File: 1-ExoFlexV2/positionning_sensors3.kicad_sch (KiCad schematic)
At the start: 34 parts, among them U63 SN74LVC1G08DBVR, U64 SN74LVC1G08DBVR, U65 SN74LVC3G14DCUT_V2

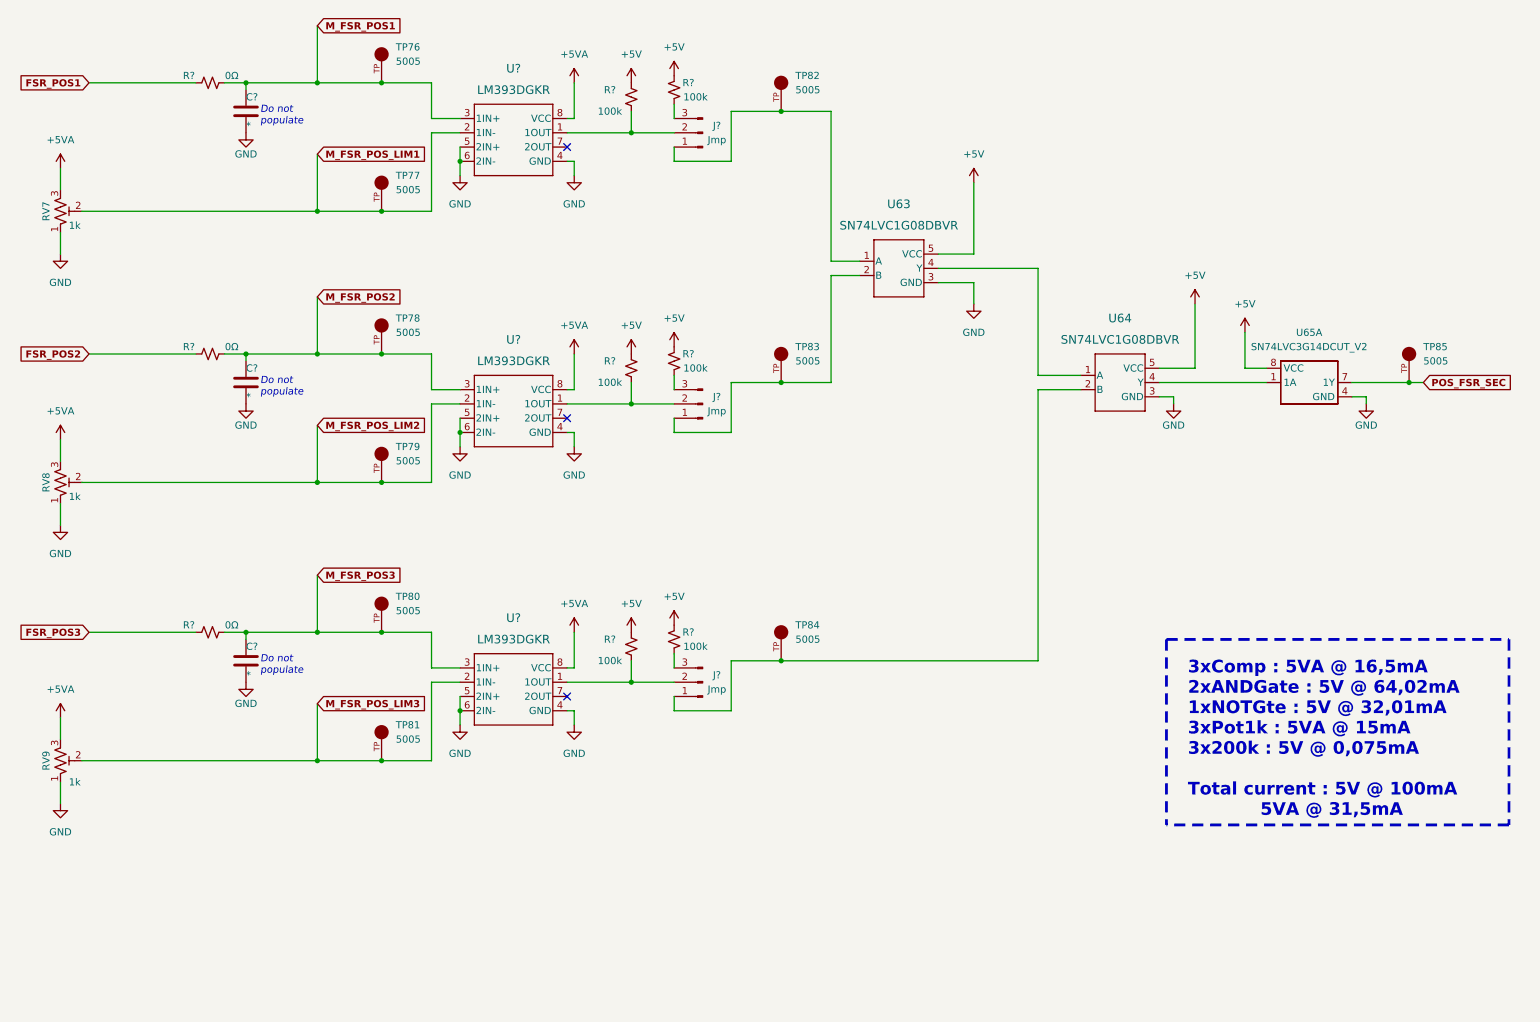
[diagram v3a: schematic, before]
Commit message: Test points et notes
- Ajout de tous les tests point nécessaires
-  Ajoute des sections de notes dans chaque page
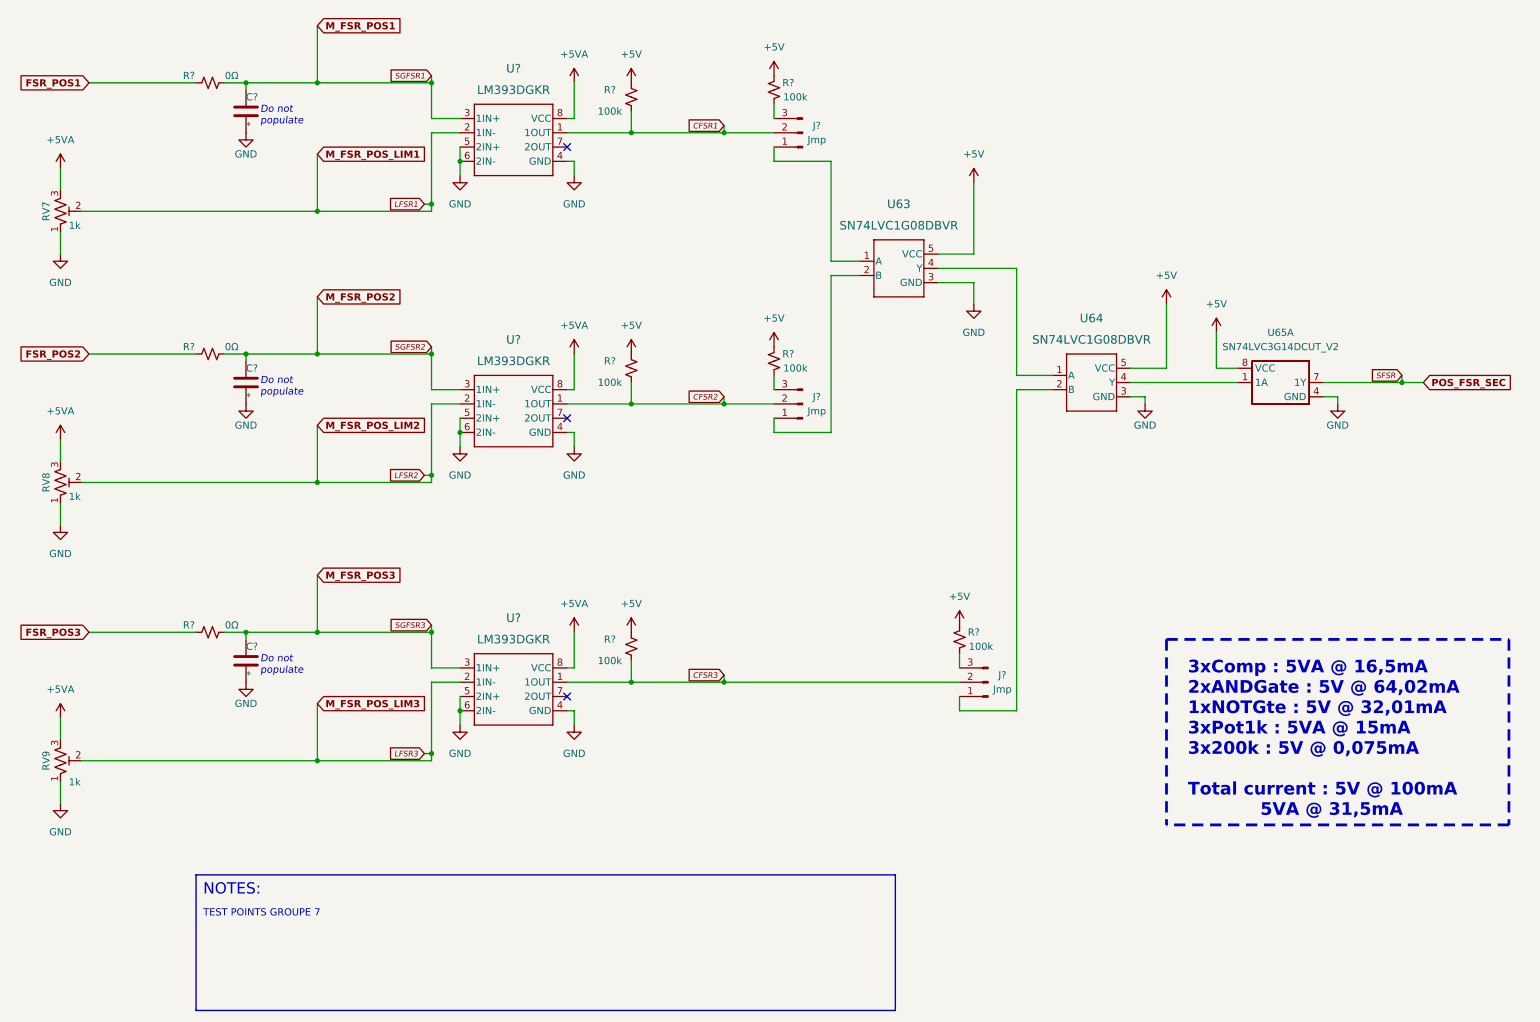
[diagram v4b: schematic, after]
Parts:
- removed TP76, TP77, TP78, TP79, TP80, TP81, TP82, TP83, TP84, TP85: 5005, FootPrint:KEYSTONE_5005, symbol SymLib:5005
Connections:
- net CFSR3: now reaches J?.2 (Pin_2), R?.2, U?.1 (1OUT)
- net CFSR2: now reaches J?.2 (Pin_2), R?.2, U?.1 (1OUT)
- net CFSR1: now reaches J?.2 (Pin_2), R?.2, U?.1 (1OUT)
- net M_FSR_POS_LIM1 renamed LFSR1
- net M_FSR_POS_LIM2 renamed LFSR2
- net M_FSR_POS_LIM3 renamed LFSR3
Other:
- note added: "NOTES:"
- note added: "TEST POINTS GROUPE 7"
- moved on the sheet: J?, R?, U64, U65A

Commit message: Schématisation terminée
- Schéma terminé
- Passage vers le PCB
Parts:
- C49, C50, C51: renamed from C?; value * -> 10nF 10V X5R; footprint Capacitor_SMD:C_0805_2012Metric -> Capacitor_SMD:C_01005_0402Metric; DESCRIPTION (none) -> 10000 pF ±10% 10V Ceramic Capacitor X5R 01005 (0402 Metric); MANUFACTURER (none) -> Murata Electronics; NOTES (none) -> DO NOT POPULATE; PACKAGE (none) -> 01005 (0402 Metric); PART NUMBER (none) -> GRM022R61A103KE19L; TYPE (none) -> SMD
- J106, J107, J108: renamed from J?; value Jmp -> Jumper; footprint (none) -> Connector_PinSocket_2.54mm:PinSocket_1x03_P2.54mm_Vertical; DESCRIPTION (none) -> CONN HEADER VERT 3POS 2.54MM; MANUFACTURER (none) -> Würth Elektronik; PACKAGE (none) -> Square 0.100" (2.54mm); PART NUMBER (none) -> 61300311121; TYPE (none) -> Through Hole
- R155, R156, R157: renamed from R?; DESCRIPTION (none) -> 0 Ohms Jumper Chip Resistor 0805 (2012 Metric) Automotive A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; MANUFACTURER (none) -> Panasonic Electronic Components; PACKAGE (none) -> 0805 (2012 Metric); PART NUMBER (none) -> ERJ-6GEY0R00V; TYPE (none) -> SMD
- R158, R159, R160, R161, R162, R163: renamed from R?; value 100k -> 100k 5% 1/8W; DESCRIPTION (none) -> 100 kOhms ±5% 0.125W, 1/8W Chip Resistor 0805 (2012 Metric)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; MANUFACTURER (none) -> Panasonic Electronic Components; PACKAGE (none) -> 0805 (2012 Metric); PART NUMBER (none) -> ERJ-6GEYJ104V; TYPE (none) -> SMD
- RV30: renamed from RV7; value 1k -> Trim 1k; DESCRIPTION (none) -> Trimmer 1k 0,5W PC PIN TOP; MANUFACTURER (none) -> Bourns Inc.; PACKAGE (none) -> Rectangular - 0.275" x 0.260" Face; PART NUMBER (none) -> 3362P-1-102LF; TYPE (none) -> Through Hole
- RV31: renamed from RV8; value 1k -> Trim 1k; DESCRIPTION (none) -> Trimmer 1k 0,5W PC PIN TOP; MANUFACTURER (none) -> Bourns Inc.; PACKAGE (none) -> Rectangular - 0.275" x 0.260" Face; PART NUMBER (none) -> 3362P-1-102LF; TYPE (none) -> Through Hole
- RV32: renamed from RV9; value 1k -> Trim 1k; DESCRIPTION (none) -> Trimmer 1k 0,5W PC PIN TOP; MANUFACTURER (none) -> Bourns Inc.; PACKAGE (none) -> Rectangular - 0.275" x 0.260" Face; PART NUMBER (none) -> 3362P-1-102LF; TYPE (none) -> Through Hole
- U79, U80, U81: renamed from U?; value LM393DGKR -> COMP; footprint DGK8 -> FootPrint:DGK8; DESCRIPTION (none) -> Comparator General Purpose Open-Collector, Rail-to-Rail 8-V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; MANUFACTURER (none) -> Texas Instruments; PACKAGE (none) -> 8-TSSOP, 8-MSOP (0.118", 3.00mm Width); PART NUMBER (none) -> LM393DGKR; TYPE (none) -> SMD
- U82: renamed from U63; value SN74LVC1G08DBVR -> AND Gate; DESCRIPTION (none) -> AND Gate IC 1 Channel SOT-23-5; MANUFACTURER (none) -> Texas Instruments; PACKAGE (none) -> SC-74A, SOT-753; PART NUMBER (none) -> SN74LVC1G08DBVR; TYPE (none) -> SMD
- U83: renamed from U64; value SN74LVC1G08DBVR -> AND Gate; DESCRIPTION (none) -> AND Gate IC 1 Channel SOT-23-5; MANUFACTURER (none) -> Texas Instruments; PACKAGE (none) -> SC-74A, SOT-753; PART NUMBER (none) -> SN74LVC1G08DBVR; TYPE (none) -> SMD
- U84: renamed from U65; value SN74LVC3G14DCUT_V2 -> Inverter; DESCRIPTION (none) -> Inverter IC 3 Channel Schmitt Trigger 8-VSSOP; MANUFACTURER (none) -> Texas Instruments; PACKAGE (none) -> 8-VFSOP (0.091", 2.30mm Width); PART NUMBER (none) -> SN74LVC3G14DCUT; TYPE (none) -> SMD
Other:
- note added: "3xComp : 5VA @ 77,4mA 2xANDGate : 5V @ 64,02mA 1xNOTGte : 5V @ 32,01mA 3xPot1k : 5VA @ 300mA 6x100k : 5V @ 0,3mA Total current : 5V @ 101mA 5VA @ 382mA"
- note removed: "3xComp : 5VA @ 16,5mA 2xANDGate : 5V @ 64,02mA 1xNOTGte : 5V @ 32,01mA 3xPot1k : 5VA @ 15mA 3x200k : 5V @ 0,075mA Total current : 5V @ 100mA 5VA @ 31,5mA"
- moved on the sheet: J106, J108, R158, R161, R163

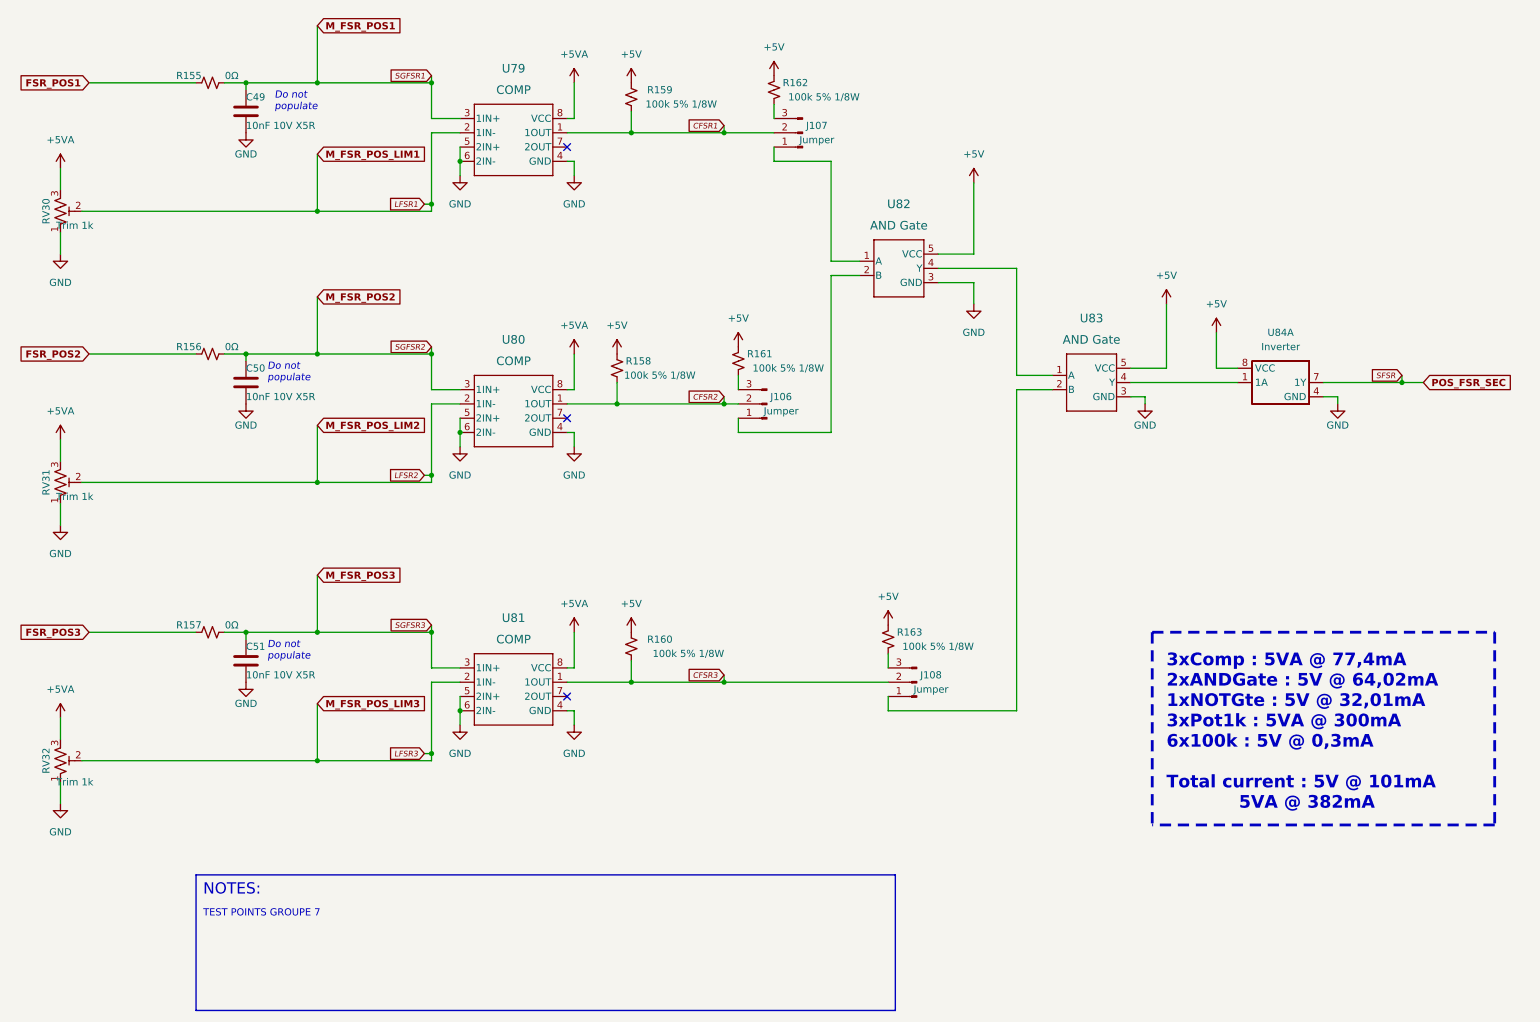
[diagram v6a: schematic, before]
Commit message: Finalisation 3
- Changement des régulateur de tension
- Retrait de test point inutile
- Changement de jumper mal positionner
- Ajout de Mounting holes et fiducial
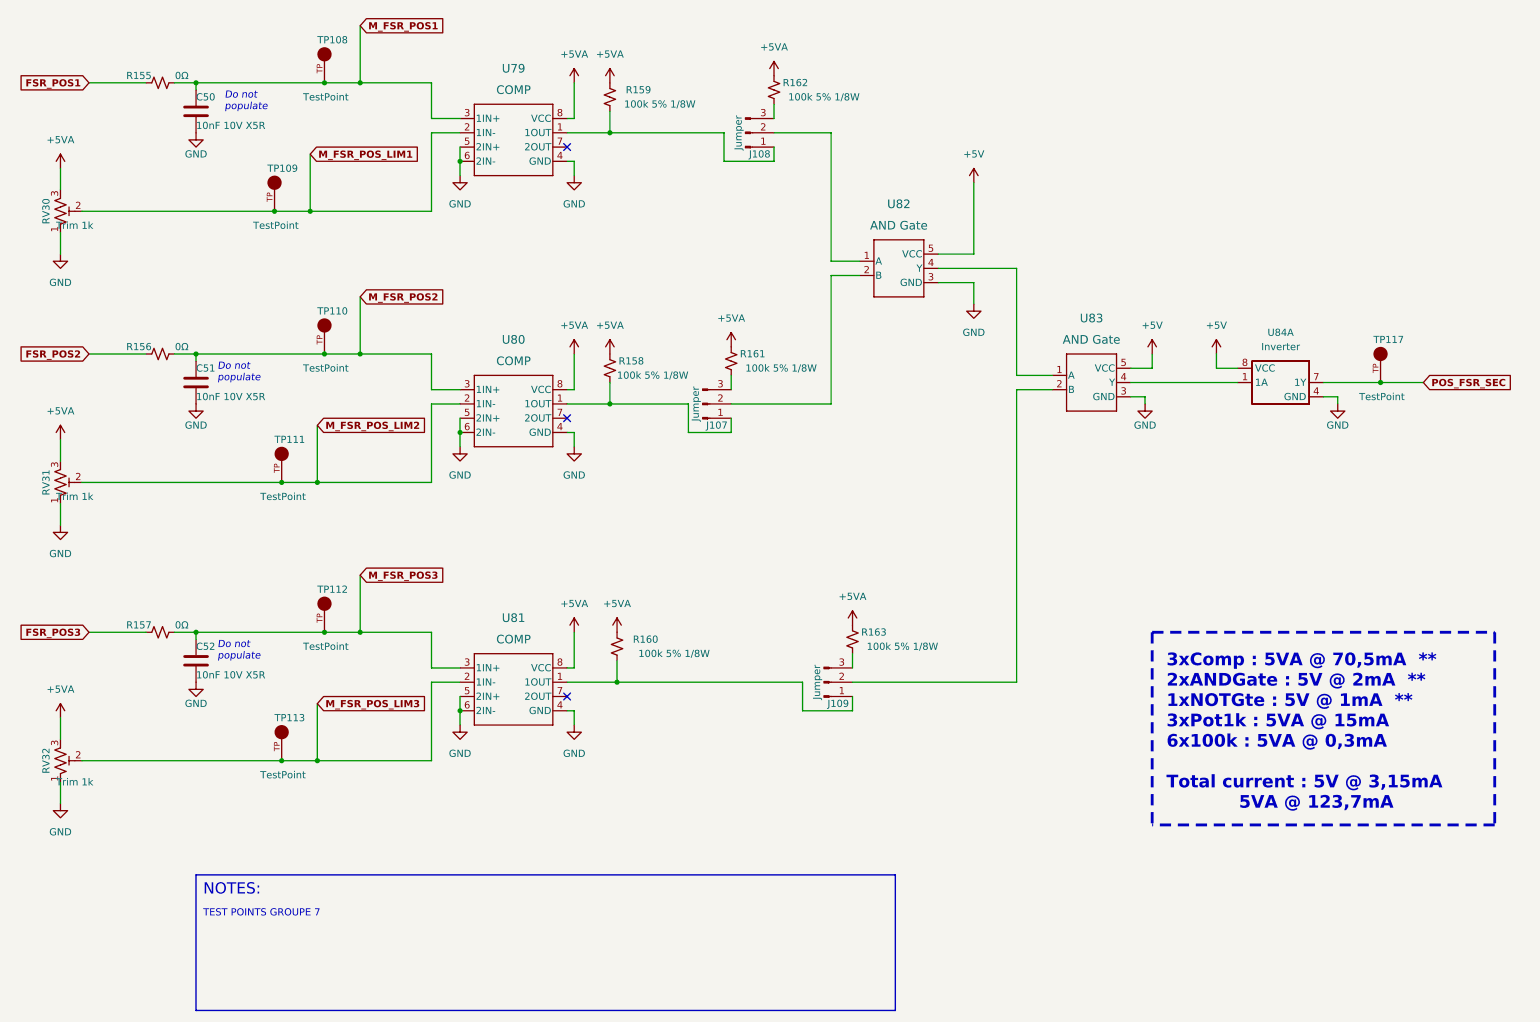
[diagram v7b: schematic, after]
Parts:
- removed C49: 10nF 10V X5R, Capacitor_SMD:C_01005_0402Metric, symbol Device:C
- added C52: 10nF 10V X5R, Capacitor_SMD:C_0603_1608Metric, symbol Device:C
- added TP108, TP109, TP110, TP111, TP112, TP113, TP117: TestPoint, FootPrint:KEYSTONE_5005, symbol SymLib:5005
- C50, C51: footprint Capacitor_SMD:C_01005_0402Metric -> Capacitor_SMD:C_0603_1608Metric; DESCRIPTION 10000 pF ±10% 10V Ceramic Capacitor X5R 01005 (0402 Metric) -> 10000 pF ±5% 10V Ceramic Capacitor U2J 0603 (1608 Metric); PACKAGE 01005 (0402 Metric) -> 0603 (1608 Metric); PART NUMBER GRM022R61A103KE19L -> GRM1857U1A103JA44D
- J107: renamed from J106; footprint Connector_PinSocket_2.54mm:PinSocket_1x03_P2.54mm_Vertical -> Connector_PinHeader_2.54mm:PinHeader_1x03_P2.54mm_Vertical
- J108: renamed from J107; footprint Connector_PinSocket_2.54mm:PinSocket_1x03_P2.54mm_Vertical -> Connector_PinHeader_2.54mm:PinHeader_1x03_P2.54mm_Vertical
- J109: renamed from J108; footprint Connector_PinSocket_2.54mm:PinSocket_1x03_P2.54mm_Vertical -> Connector_PinHeader_2.54mm:PinHeader_1x03_P2.54mm_Vertical
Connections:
- net +5V: no longer R158.1, R159.1, R160.1, R161.2, R162.2, R163.2
- net +5VA: now also R158.1, R159.1, R160.1, R161.2, R162.2, R163.2
- net GND: now also C52.2
- net M_FSR_POS1: now also C50.1, TP108.TP
- net M_FSR_POS2: now also C51.1, TP110.TP; no longer C50.1
- net M_FSR_POS3: now also C52.1, TP112.TP; no longer C51.1
- net POS_FSR_SEC: now also TP117.TP
- net at J107.1 (Pin_1): now also R158.2, U80.1 (1OUT); no longer U82.2 (B)
- net at J109.1 (Pin_1): now also R160.2, U81.1 (1OUT); no longer U83.2 (B)
- net at J108.1 (Pin_1): now also R159.2, U79.1 (1OUT); no longer U82.1 (A)
- removed net CFSR1: J108.2 (Pin_2), R159.2, U79.1 (1OUT)
- removed net CFSR2: J107.2 (Pin_2), R158.2, U80.1 (1OUT)
- removed net CFSR3: J109.2 (Pin_2), R160.2, U81.1 (1OUT)
- net LFSR1 renamed M_FSR_POS_LIM1
- net M_FSR_POS_LIM1: now also TP109.TP
- net LFSR2 renamed M_FSR_POS_LIM2
- net M_FSR_POS_LIM2: now also TP111.TP
- net LFSR3 renamed M_FSR_POS_LIM3
- net M_FSR_POS_LIM3: now also TP113.TP
- new net: J107.2 (Pin_2), U82.2 (B)
- new net: J109.2 (Pin_2), U83.2 (B)
- new net: J108.2 (Pin_2), U82.1 (A)
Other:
- note added: "3xComp : 5VA @ 70,5mA ** 2xANDGate : 5V @ 2mA ** 1xNOTGte : 5V @ 1mA ** 3xPot1k : 5VA @ 15mA 6x100k : 5VA @ 0,3mA Total current : 5V @ 3,15mA 5VA @ 123,7mA"
- note removed: "3xComp : 5VA @ 77,4mA 2xANDGate : 5V @ 64,02mA 1xNOTGte : 5V @ 32,01mA 3xPot1k : 5VA @ 300mA 6x100k : 5V @ 0,3mA Total current : 5V @ 101mA 5VA @ 382mA"
- moved on the sheet: J107, J108, J109, R155, R156, R157, R158, R159, R160, R161, R162, R163
